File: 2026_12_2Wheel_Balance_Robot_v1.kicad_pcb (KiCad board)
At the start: 2 copper layers, 73.5 x 74.5 mm, 56 parts, among them J1 Conn_01x04, J2 CONN_MPU6050, J3 USB_C_Receptacle_USB2.0_14P, J4 ESP_Conn, J5 BATT_CONN, J6 M1_CONN, J7 M2_CONN, J8 ENCODER_CONN, J9 MT6701_CONN, SW2 SW_uP_Reset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

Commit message: homework push
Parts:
- C24, J6: moved to F.Cu
- moved J3 71.1 mm to (153.7, 82.2), turned to 90 degrees
- moved R8 60.6 mm to (145.6, 78.5), turned to 180 degrees
- moved R7 53.0 mm to (144.9, 86.0), turned to 0 degrees
- moved C8 52.7 mm to (99.5, 99.5)
- moved J6 48.4 mm to (124.8, 123.5), turned to 0 degrees
- moved U5 47.8 mm to (138.5, 82.5), turned to 180 degrees
- moved F1 46.7 mm to (144.9, 89.0), turned to 180 degrees
- moved R4 45.6 mm to (133.5, 80.5), turned to 180 degrees
- moved U6 45.2 mm to (105.8, 108.0)
- moved R6 44.8 mm to (114.0, 108.0), turned to 90 degrees
- moved C13 44.8 mm to (99.7, 107.5), turned to 90 degrees
- moved R1 44.3 mm to (149.5, 95.0)
- moved C15 43.8 mm to (99.5, 112.5), turned to -90 degrees
- moved D3 43.6 mm to (116.5, 108.0), turned to -90 degrees
- moved D2 41.1 mm to (149.5, 92.5), turned to 0 degrees
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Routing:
- net VM: track 0.00 -> 48.7 mm
- net /MD_BO2: track 0.00 -> 45.3 mm, vias 0 -> 2
- net /MD_BO1: track 0.00 -> 43.2 mm, vias 0 -> 2
- net 5V_REG: track 0.00 -> 27.7 mm
- net GND: track 0.00 -> 23.6 mm, vias 0 -> 25
- net +3.3V: track 0.00 -> 19.6 mm
- net /USB_D-: track 0.00 -> 13.5 mm
- net Net-(F1-~-Pad1): track 0.00 -> 13.3 mm
- net /USB_D+: track 0.00 -> 12.7 mm
- net Vusb: track 0.00 -> 8.92 mm
- net /WS_DIN: track 0.00 -> 8.41 mm
- net Net-(J3-CC1): track 0.00 -> 6.28 mm
- net +5V: track 0.00 -> 5.84 mm
- net /ESD_D+: track 0.00 -> 5.08 mm
- net Net-(J3-CC2): track 0.00 -> 4.91 mm
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- added copper zone on B.Cu, net GND
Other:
- board size 73.5 x 74.5 mm -> 62 x 76.2 mm

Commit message: Homework Routing
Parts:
- moved C8 49.3 mm to (148.7, 104.0), turned to 90 degrees
- moved C9 41.9 mm to (111.0, 81.0)
- moved U2 38.8 mm to (104.6, 87.0)
- moved R17 35.5 mm to (154.5, 62.0), turned to 180 degrees
- moved C6 28.1 mm to (110.5, 89.5), turned to -90 degrees
- moved J1 22.8 mm to (165.5, 66.0), turned to 0 degrees
- moved C19 22.0 mm to (125.0, 83.0)
- moved C15 20.7 mm to (120.1, 113.4), turned to 0 degrees
- moved C13 17.0 mm to (115.6, 113.4), turned to 180 degrees
- moved J8 16.3 mm to (138.0, 57.5), turned to 0 degrees
- moved Y3 15.2 mm to (121.6, 82.9), turned to 180 degrees
- moved C2 14.6 mm to (143.5, 78.5), turned to 0 degrees
- moved C1 12.7 mm to (128.2, 77.4)
- moved C14 12.7 mm to (124.2, 104.9)
- moved C18 12.7 mm to (151.2, 113.0)
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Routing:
- net +3.3V: track 19.6 -> 259.8 mm, vias 0 -> 10
- net +5V: track 5.84 -> 150.6 mm, vias 0 -> 4
- net GND: track 23.6 -> 142.7 mm, vias 25 -> 40
- net /MD_AO2: track 0.00 -> 77.1 mm
- net /MD_AO1: track 0.00 -> 73.6 mm
- net Vusb: track 8.92 -> 81.1 mm, vias 0 -> 2
- net VM: track 48.7 -> 107.0 mm, vias 0 -> 2
- net /MD_PWMB: track 0.00 -> 45.4 mm, vias 0 -> 2
- net /ESP_TX: track 0.00 -> 44.5 mm
- net /MD_BIN2: track 0.00 -> 42.3 mm
- net /MD_BIN1: track 0.00 -> 40.6 mm
- net /MD_STBY: track 0.00 -> 37.2 mm
- net /RESET: track 0.00 -> 33.8 mm
- net /ESP_RX: track 0.00 -> 33.5 mm
- net /SWCLK: track 0.00 -> 31.0 mm, vias 0 -> 2
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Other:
- board size 62 x 76.2 mm -> 75 x 75 mm
- board text added: "Ryan Kearns ENCEE 3231 Denver University"

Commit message: Changed a route
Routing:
- net /MD_BO1: track 70.6 -> 40.6 mm, vias 2 -> 0
- net /MD_BO2: track 65.1 -> 41.5 mm, vias 2 -> 0
- net +5V: track 150.6 -> 151.4 mm, vias 4 -> 6

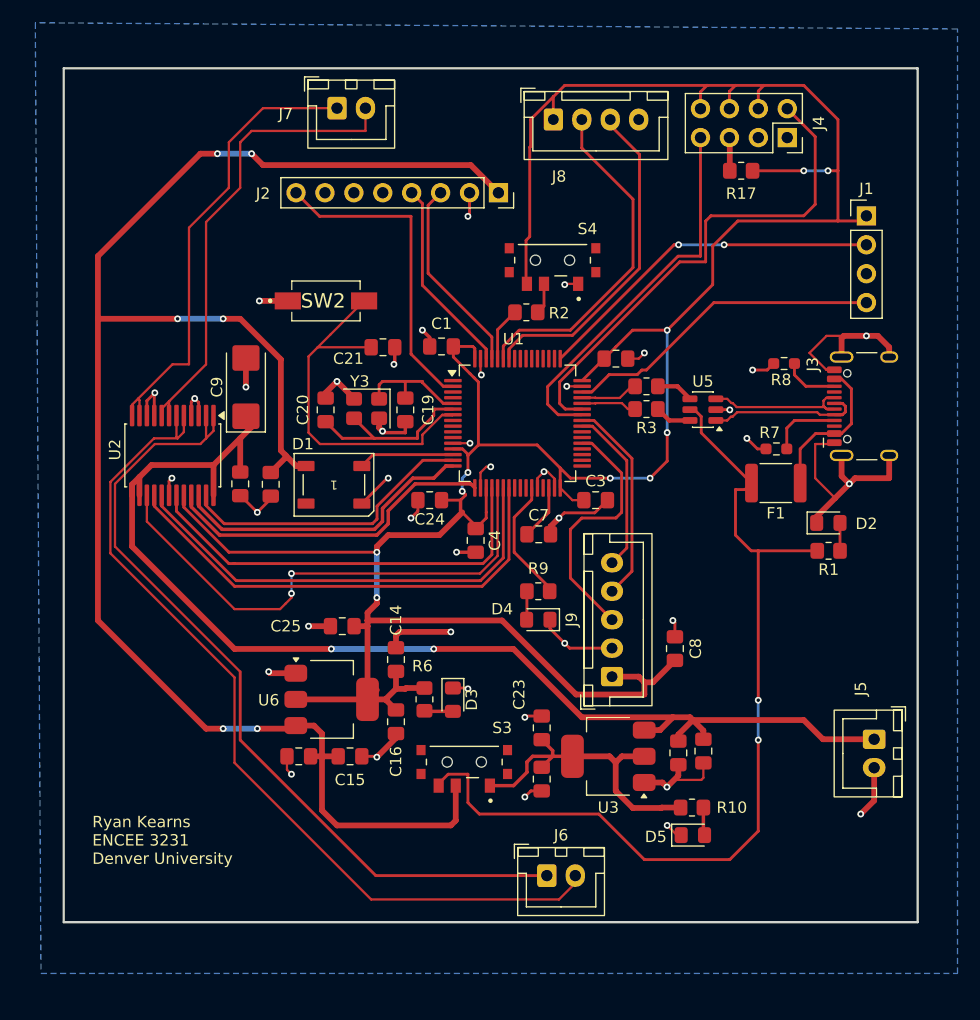
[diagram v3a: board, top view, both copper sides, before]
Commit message: Changed 3V route
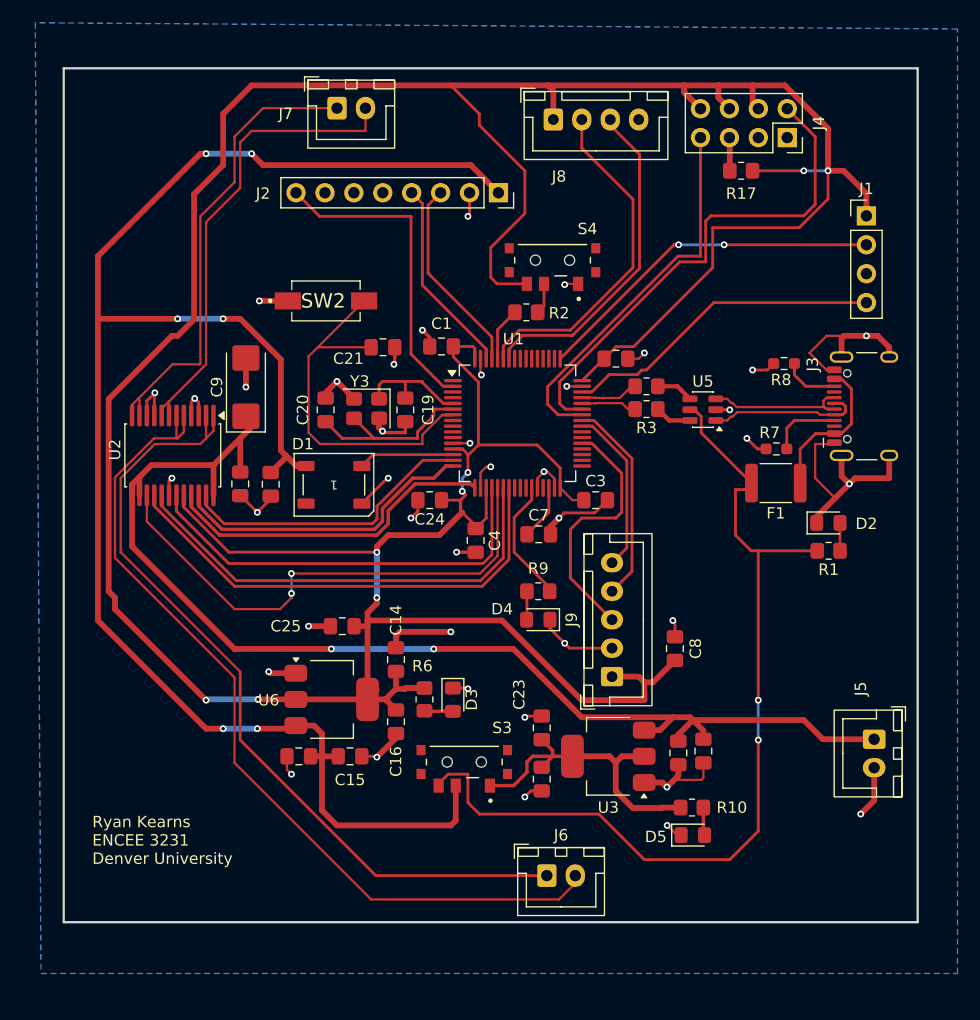
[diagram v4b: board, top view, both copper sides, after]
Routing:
- net +3.3V: track 259.8 -> 343.6 mm, vias 10 -> 8
- net /MD_BO1: track 40.6 -> 41.2 mm

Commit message: Updated Gerbers to include mounting holes
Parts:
- added H1: M2, MountingHole:MountingHole_2.2mm_M2, F.Cu at (99.5, 123.5)
- added H2: M2, MountingHole:MountingHole_2.2mm_M2, F.Cu at (166.0, 124.5)
- added H3: M2, MountingHole:MountingHole_2.2mm_M2, F.Cu at (98.5, 57.5)
- added H4: M2, MountingHole:MountingHole_2.2mm_M2, F.Cu at (166.0, 57.5)
